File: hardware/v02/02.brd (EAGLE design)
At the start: 79.7 x 38.1 mm, 29 parts, among them IC2 78L05Z, IC3 MSP430G2553, X2 RJ45-6L-B

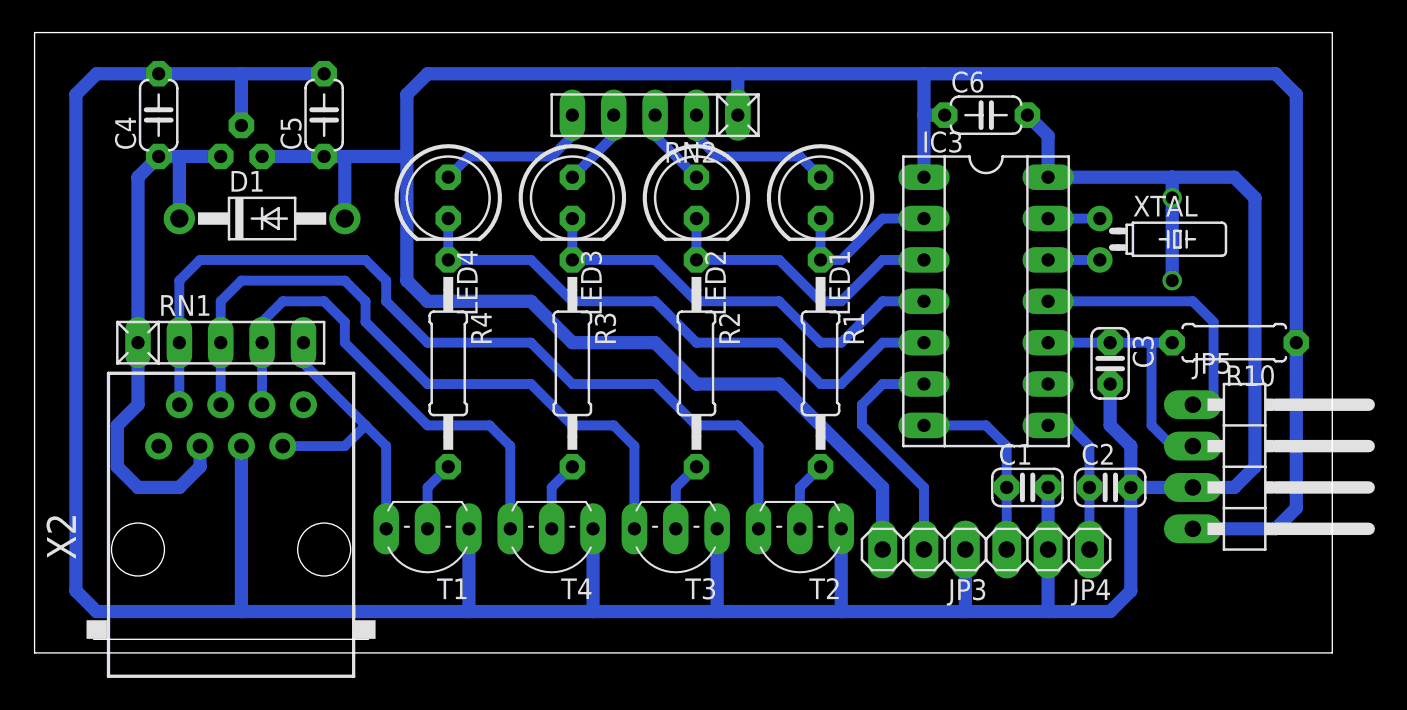
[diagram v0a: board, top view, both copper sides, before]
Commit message: echange pin header; labels on top
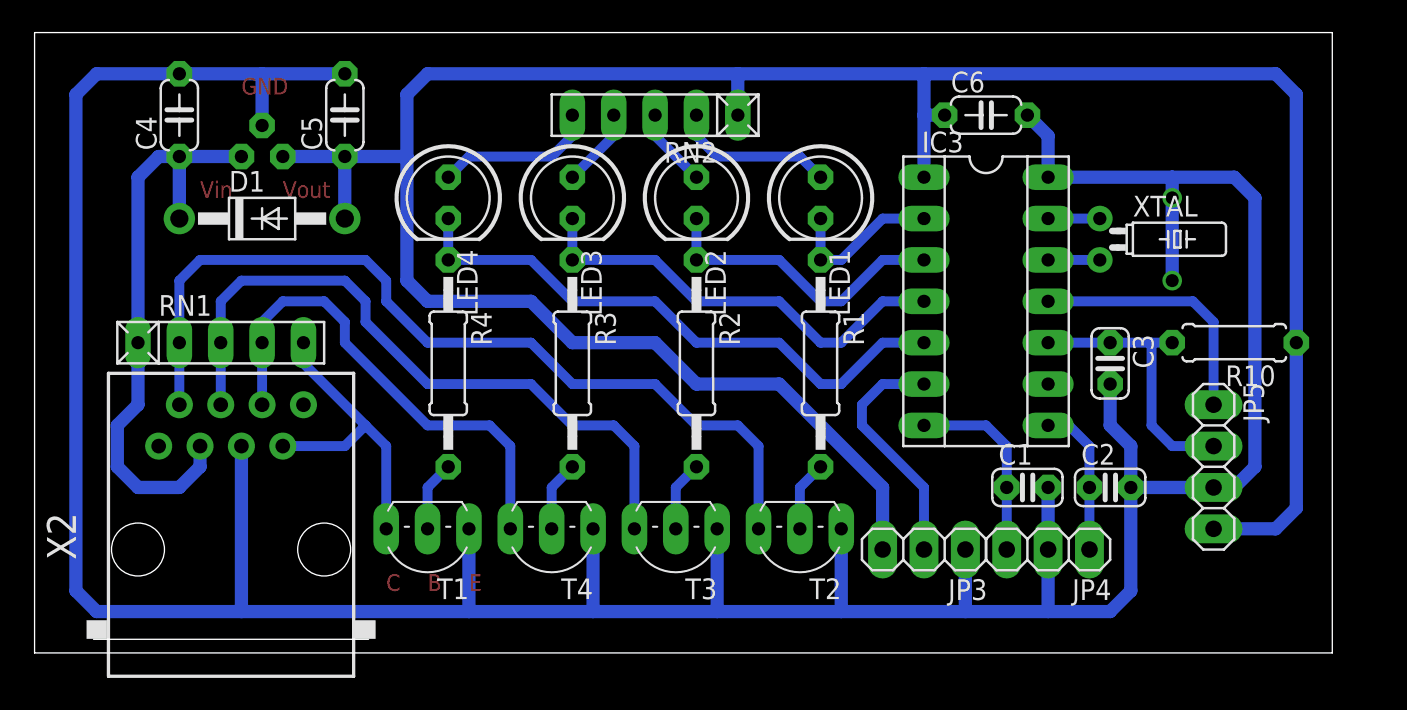
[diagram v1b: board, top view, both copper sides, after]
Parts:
- JP5: device pinhead:1X04/90 -> pinhead:1X04
- moved JP5 2.54 mm to (72.4, 11.4)
- moved IC2 1.27 mm to (14.0, 30.5)
- moved C4 1.27 mm to (8.89, 33.0)
- moved C5 1.27 mm to (19.1, 33.0)
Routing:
- net VCC: track 161.8 -> 159.2 mm
- net GND: track 218.9 -> 220.2 mm
- net +5V: track 35.1 -> 36.4 mm
- net N$6: track 17.0 -> 15.8 mm
- net N$5: track 15.8 -> 17.0 mm
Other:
- board text added: "B"
- board text added: "C"
- board text added: "E"
- board text added: "GND"
- board text added: "Vin"
- board text added: "Vout"
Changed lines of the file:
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@@
 <?xml version="1.0" encoding="utf-8"?>
 <!DOCTYPE eagle SYSTEM "eagle.dtd">
-<eagle version="7.3.0">
+<eagle version="6.6.0">
 <drawing>
 <settings>
@@
 <wire x1="79.68" y1="38.09" x2="0" y2="38.09" width="0" layer="20"/>
 <wire x1="0" y1="38.09" x2="0" y2="0" width="0" layer="20"/>
-<dimension x1="0" y1="38.09" x2="79.68" y2="38.09" x3="39.84" y3="39.37" textsize="1.778" layer="1"/>
-<dimension x1="79.68" y1="38.09" x2="79.68" y2="0" x3="82.550003125" y3="19.045" textsize="1.778" layer="1"/>
+<text x="12.7" y="34.29" size="1.016" layer="1">GND</text>
+<text x="10.16" y="27.94" size="1.016" layer="1">Vin</text>
+<text x="15.24" y="27.94" size="1.016" layer="1">Vout</text>
+<text x="26.67" y="3.81" size="1.016" layer="1">E</text>
+<text x="24.13" y="3.81" size="1.016" layer="1">B</text>
+<text x="21.59" y="3.81" size="1.016" layer="1">C</text>
 </plain>
 <attributes>
@@
 <pass name="Default">
 <param name="RoutingGrid" value="50mil"/>
-<param name="AutoGrid" value="1"/>
-<param name="Efforts" value="0"/>
-<param name="TopRouterVariant" value="1"/>
 <param name="tpViaShape" value="round"/>
 <param name="PrefDir.1" value="|"/>
@@
 <element name="R4" library="rcl" package="0207/12" value="470" x="25.4" y="17.78" rot="R270"/>
 <element name="LED4" library="led" package="LED5MM" value="" x="25.4" y="27.94" rot="R270"/>
-<element name="IC2" library="linear" package="TO92" value="78L05Z" x="12.7" y="30.48" rot="MR0"/>
+<element name="IC2" library="linear" package="TO92" value="78L05Z" x="13.97" y="30.48" rot="MR0"/>
 <element name="T1" library="transistor" package="TO92-EBC" value="" x="24.13" y="6.35" rot="R180"/>
 <element name="R1" library="rcl" package="0207/12" value="470" x="48.26" y="17.78" rot="R270"/>
@@
 <element name="JP3" library="pinhead" package="1X03" value="" x="54.61" y="6.35" rot="R180"/>
 <element name="JP4" library="pinhead" package="1X03" value="" x="62.23" y="6.35" rot="R180"/>
-<element name="JP5" library="pinhead" package="1X04/90" value="" x="74.93" y="11.43" rot="R270"/>
+<element name="JP5" library="pinhead" package="1X04" value="" x="72.39" y="11.43" rot="R270"/>
 <element name="X2" library="con-tycoelectronics" package="RJ45-NO-SHIELD" value="RJ45-6L-B" x="12.065" y="6.35">
 <attribute name="MF" value="" x="12.065" y="6.35" size="1.778" layer="27" display="off"/>
@@
 </element>
 <element name="IC3" library="ic-package" package="SOCKET-14" value="MSP430G2553" x="58.42" y="21.59" rot="R270"/>
-<element name="C4" library="rcl" package="C050-024X044" value="330nF" x="7.62" y="33.02" rot="R90"/>
-<element name="C5" library="rcl" package="C050-024X044" value="100nF" x="17.78" y="33.02" rot="R90"/>
+<element name="C4" library="rcl" package="C050-024X044" value="330nF" x="8.89" y="33.02" rot="R90"/>
+<element name="C5" library="rcl" package="C050-024X044" value="100nF" x="19.05" y="33.02" rot="R90"/>
 <element name="C6" library="rcl" package="C050-024X044" value="100nF" x="58.42" y="33.02"/>
 <element name="D1" library="adafruit" package="DO41-10" value="1N4004" x="13.97" y="26.67"/>
@@
 <wire x1="22.86" y1="22.86" x2="22.86" y2="30.48" width="0.8128" layer="16"/>
 <wire x1="22.86" y1="30.48" x2="22.86" y2="34.29" width="0.8128" layer="16"/>
-<wire x1="71.12" y1="7.62" x2="76.2" y2="7.62" width="0.8128" layer="16"/>
+<wire x1="72.39" y1="7.62" x2="76.2" y2="7.62" width="0.8128" layer="16"/>
 <wire x1="76.2" y1="7.62" x2="77.47" y2="8.89" width="0.8128" layer="16"/>
 <contactref element="C5" pad="1"/>
 <contactref element="C6" pad="1"/>
 <wire x1="55.88" y1="33.02" x2="54.61" y2="33.02" width="0.8128" layer="16"/>
-<wire x1="13.97" y1="30.48" x2="17.78" y2="30.48" width="0.8128" layer="16"/>
-<wire x1="17.78" y1="30.48" x2="19.05" y2="30.48" width="0.8128" layer="16"/>
+<wire x1="15.24" y1="30.48" x2="19.05" y2="30.48" width="0.8128" layer="16"/>
 <contactref element="D1" pad="A"/>
 <wire x1="19.05" y1="30.48" x2="22.86" y2="30.48" width="0.8128" layer="16"/>
@@
 <contactref element="JP5" pad="3"/>
 <contactref element="C3" pad="2"/>
-<wire x1="12.7" y1="32.385" x2="12.7" y2="35.56" width="0.8128" layer="16"/>
+<wire x1="13.97" y1="32.385" x2="13.97" y2="35.56" width="0.8128" layer="16"/>
 <wire x1="62.23" y1="2.54" x2="57.15" y2="2.54" width="0.8128" layer="16"/>
 <wire x1="57.15" y1="2.54" x2="57.15" y2="6.35" width="0.8128" layer="16"/>
@@
 <wire x1="62.23" y1="10.16" x2="62.23" y2="6.35" width="0.8128" layer="16"/>
 <wire x1="74.93" y1="11.43" x2="73.66" y2="10.16" width="0.8128" layer="16"/>
-<wire x1="73.66" y1="10.16" x2="71.12" y2="10.16" width="0.8128" layer="16"/>
+<wire x1="73.66" y1="10.16" x2="72.39" y2="10.16" width="0.8128" layer="16"/>
 <contactref element="C4" pad="2"/>
 <contactref element="C5" pad="2"/>
@@
 <wire x1="60.96" y1="33.02" x2="62.23" y2="31.75" width="0.8128" layer="16"/>
 <wire x1="62.23" y1="31.75" x2="62.23" y2="29.21" width="0.8128" layer="16"/>
-<wire x1="3.81" y1="35.56" x2="7.62" y2="35.56" width="0.8128" layer="16"/>
-<wire x1="7.62" y1="35.56" x2="12.7" y2="35.56" width="0.8128" layer="16"/>
-<wire x1="12.7" y1="35.56" x2="17.78" y2="35.56" width="0.8128" layer="16"/>
-<wire x1="71.12" y1="10.16" x2="67.31" y2="10.16" width="0.8128" layer="16"/>
+<wire x1="3.81" y1="35.56" x2="8.89" y2="35.56" width="0.8128" layer="16"/>
+<wire x1="8.89" y1="35.56" x2="13.97" y2="35.56" width="0.8128" layer="16"/>
+<wire x1="13.97" y1="35.56" x2="19.05" y2="35.56" width="0.8128" layer="16"/>
+<wire x1="72.39" y1="10.16" x2="67.31" y2="10.16" width="0.8128" layer="16"/>
 </signal>
 <signal name="N$3">
@@
 <wire x1="68.58" y1="19.05" x2="68.58" y2="13.97" width="0.6096" layer="16"/>
 <wire x1="68.58" y1="13.97" x2="69.85" y2="12.7" width="0.6096" layer="16"/>
-<wire x1="69.85" y1="12.7" x2="71.12" y2="12.7" width="0.6096" layer="16"/>
+<wire x1="69.85" y1="12.7" x2="72.39" y2="12.7" width="0.6096" layer="16"/>
 </signal>
 <signal name="N$6">
@@
 <wire x1="71.12" y1="21.59" x2="62.23" y2="21.59" width="0.6096" layer="16"/>
 <wire x1="72.39" y1="20.32" x2="72.39" y2="15.24" width="0.6096" layer="16"/>
-<wire x1="72.39" y1="15.24" x2="71.12" y2="15.24" width="0.6096" layer="16"/>
 </signal>
 <signal name="N$2">
@@
 <wire x1="6.35" y1="15.24" x2="6.35" y2="19.05" width="0.8128" layer="16"/>
 <contactref element="C4" pad="1"/>
-<wire x1="11.43" y1="30.48" x2="8.89" y2="30.48" width="0.8128" layer="16"/>
+<wire x1="12.7" y1="30.48" x2="8.89" y2="30.48" width="0.8128" layer="16"/>
 <wire x1="8.89" y1="30.48" x2="7.62" y2="30.48" width="0.8128" layer="16"/>
 <wire x1="7.62" y1="30.48" x2="6.35" y2="29.21" width="0.8128" layer="16"/>

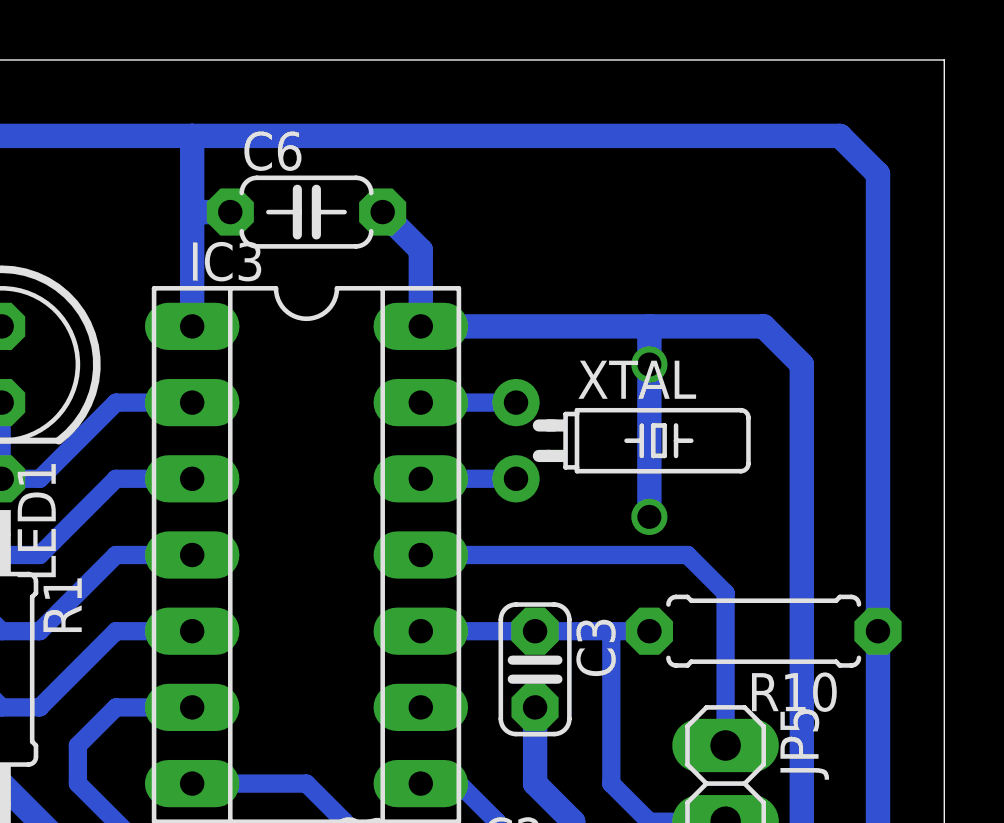
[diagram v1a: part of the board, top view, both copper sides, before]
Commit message: reroute wires for optional mounting holes; XTAL GND plane
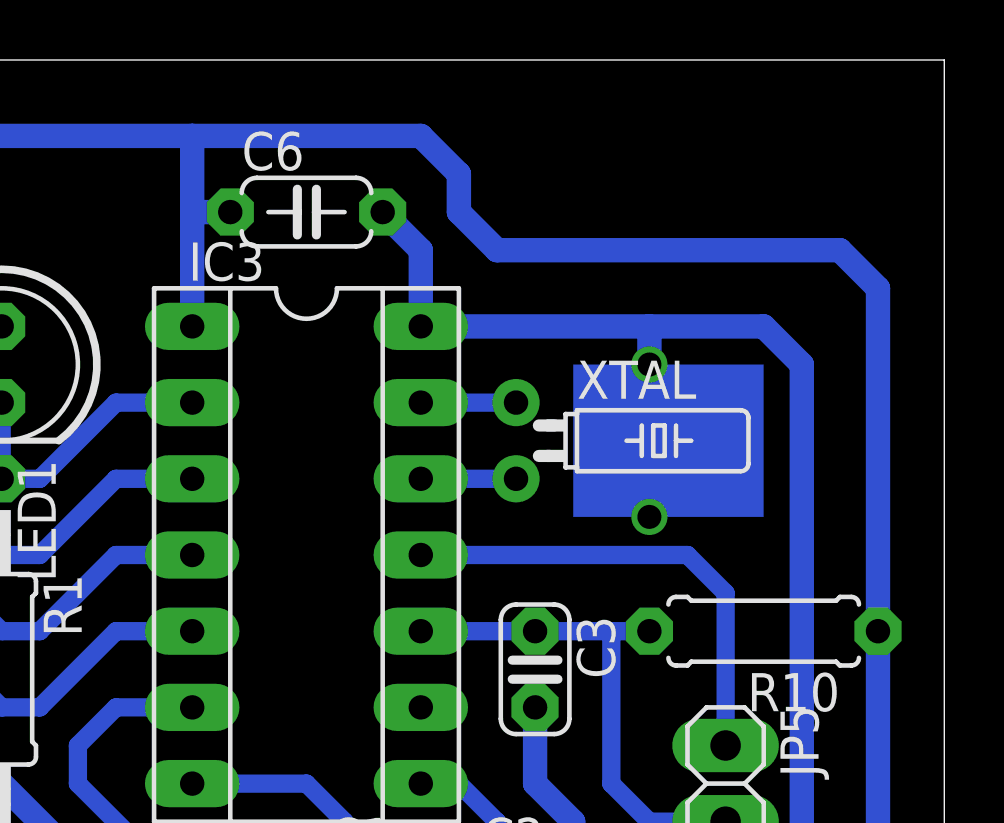
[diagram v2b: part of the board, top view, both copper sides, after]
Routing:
- net VCC: track 159.2 -> 157.8 mm
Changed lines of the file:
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@@
 <?xml version="1.0" encoding="utf-8"?>
 <!DOCTYPE eagle SYSTEM "eagle.dtd">
-<eagle version="6.6.0">
+<eagle version="6.5.0">
 <drawing>
 <settings>
@@
 <layer number="43" name="vRestrict" color="2" fill="10" visible="yes" active="yes"/>
 <layer number="44" name="Drills" color="7" fill="1" visible="no" active="yes"/>
-<layer number="45" name="Holes" color="7" fill="1" visible="no" active="yes"/>
+<layer number="45" name="Holes" color="7" fill="1" visible="yes" active="yes"/>
 <layer number="46" name="Milling" color="3" fill="1" visible="no" active="yes"/>
 <layer number="47" name="Measures" color="7" fill="1" visible="no" active="yes"/>
@@
 <text x="24.13" y="3.81" size="1.016" layer="1">B</text>
 <text x="21.59" y="3.81" size="1.016" layer="1">C</text>
+<rectangle x1="67.31" y1="22.86" x2="73.66" y2="27.94" layer="16"/>
 </plain>
 <attributes>
@@
 <contactref element="JP5" pad="4"/>
 <wire x1="77.47" y1="8.89" x2="77.47" y2="19.05" width="0.8128" layer="16"/>
-<wire x1="77.47" y1="19.05" x2="77.47" y2="34.29" width="0.8128" layer="16"/>
-<wire x1="77.47" y1="34.29" x2="76.2" y2="35.56" width="0.8128" layer="16"/>
-<wire x1="76.2" y1="35.56" x2="54.61" y2="35.56" width="0.8128" layer="16"/>
+<wire x1="77.47" y1="19.05" x2="77.47" y2="30.48" width="0.8128" layer="16"/>
+<wire x1="77.47" y1="30.48" x2="76.2" y2="31.75" width="0.8128" layer="16"/>
+<wire x1="76.2" y1="31.75" x2="64.77" y2="31.75" width="0.8128" layer="16"/>
+<wire x1="64.77" y1="31.75" x2="63.5" y2="33.02" width="0.8128" layer="16"/>
+<wire x1="63.5" y1="33.02" x2="63.5" y2="34.29" width="0.8128" layer="16"/>
+<wire x1="63.5" y1="34.29" x2="62.23" y2="35.56" width="0.8128" layer="16"/>
+<wire x1="62.23" y1="35.56" x2="54.61" y2="35.56" width="0.8128" layer="16"/>
 <wire x1="22.86" y1="34.29" x2="24.13" y2="35.56" width="0.8128" layer="16"/>
 <wire x1="24.13" y1="35.56" x2="43.18" y2="35.56" width="0.8128" layer="16"/>
